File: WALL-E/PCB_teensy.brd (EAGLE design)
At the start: 128 x 109 mm, 44 parts

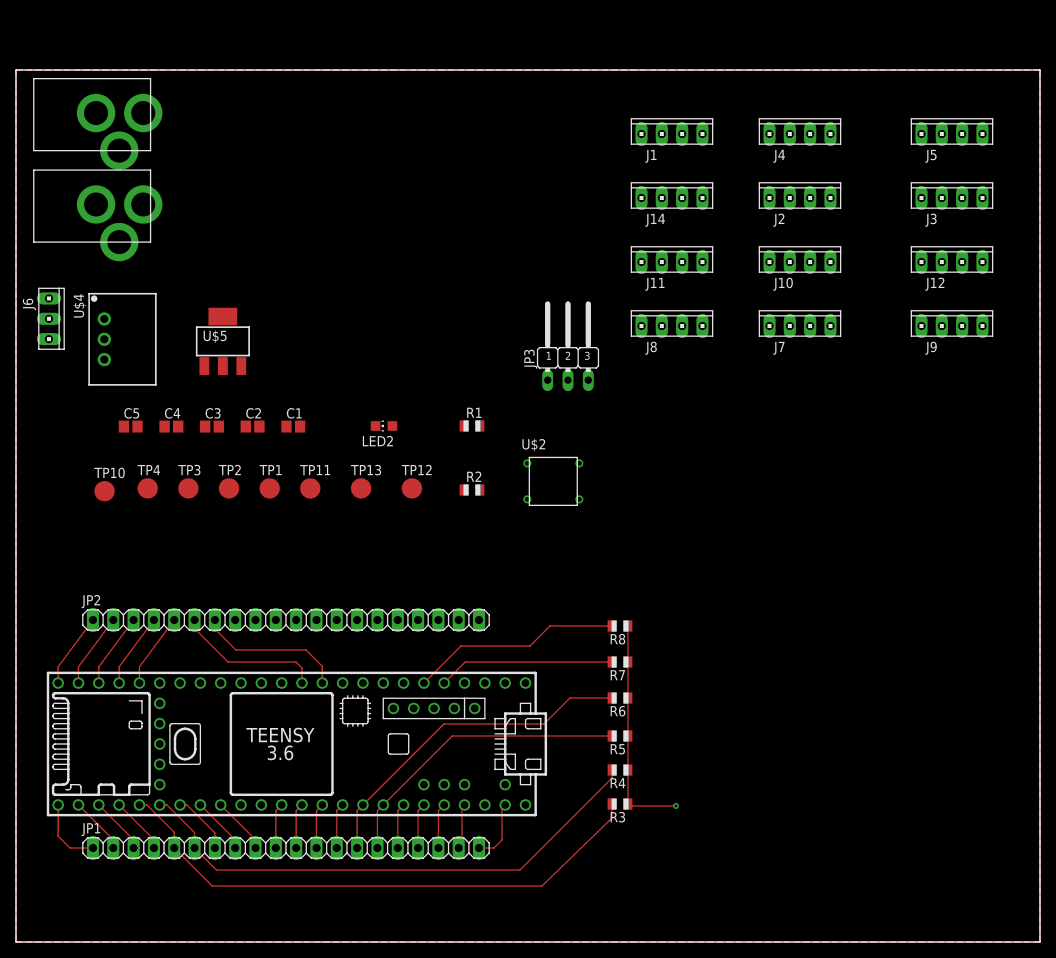
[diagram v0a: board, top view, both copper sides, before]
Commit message: Finished wiring the layers besides the tactile switch.
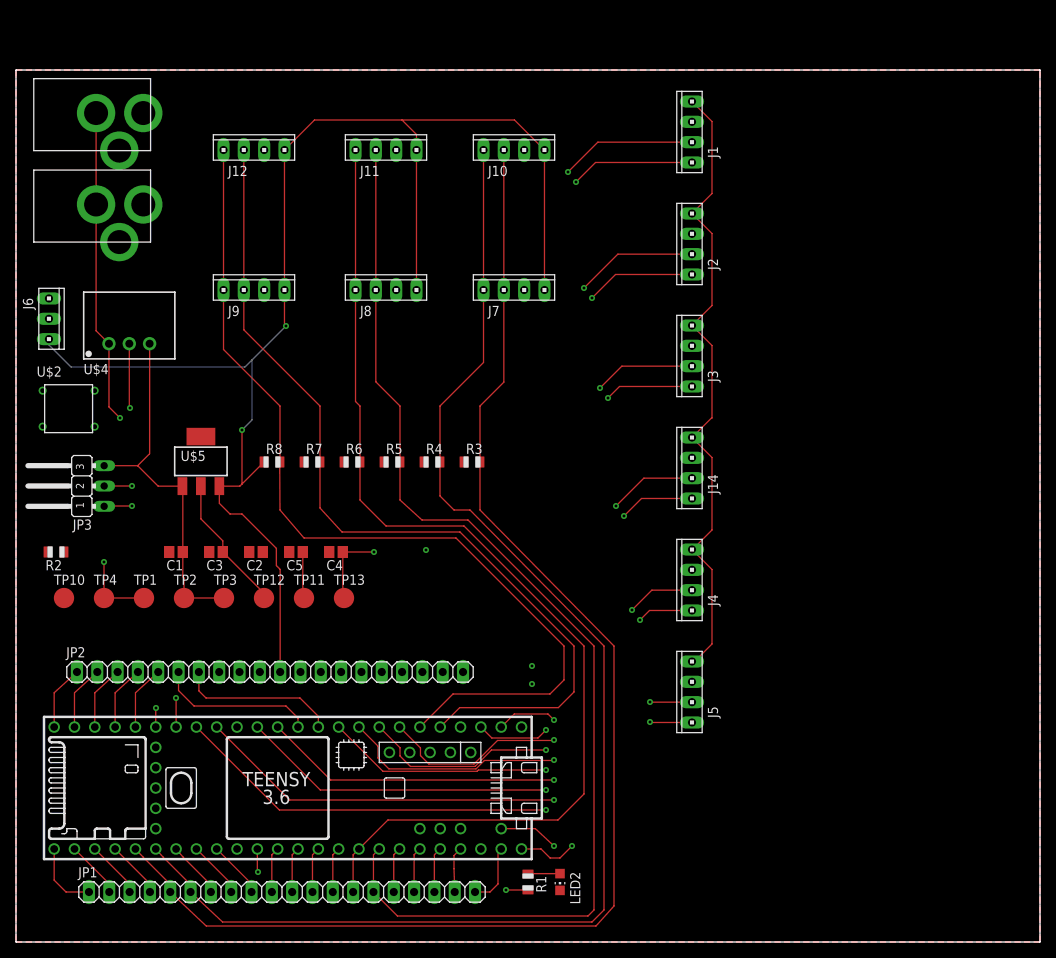
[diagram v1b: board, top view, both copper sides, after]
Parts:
- moved J12 88.4 mm to (29.8, 99.0)
- moved J9 87.4 mm to (29.8, 81.5)
- moved J5 77.0 mm to (84.5, 31.2), turned to 90 degrees
- moved U$2 61.3 mm to (3.58, 63.7)
- moved LED2 61.1 mm to (68.0, 7.50), turned to 180 degrees
- moved JP3 61.0 mm to (9.75, 57.0), turned to 90 degrees
- moved R1 57.4 mm to (64.0, 7.50), turned to 270 degrees
- moved J4 57.4 mm to (84.5, 45.2), turned to 90 degrees
- moved R2 52.6 mm to (5.00, 48.8), turned to 180 degrees
- moved R8 48.1 mm to (32.0, 60.0), turned to 0 degrees
- moved R3 46.6 mm to (57.0, 60.0), turned to 0 degrees
- moved R7 45.9 mm to (37.0, 60.0), turned to 0 degrees
- moved R4 45.1 mm to (52.0, 60.0), turned to 0 degrees
- moved R6 44.6 mm to (42.0, 60.0), turned to 0 degrees
- moved R5 44.6 mm to (47.0, 60.0), turned to 0 degrees
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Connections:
- net 10U renamed 10CS
- net 14U renamed A0
- net 15U renamed A1
- net 16U renamed A2
- net 17U renamed A3
- net 20U renamed A6
- net 21U renamed A7
- net 22U renamed A8
- net 23U renamed A9
- net 31U renamed A12
- net 32U renamed A13
- net 9U renamed 9CS
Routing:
- net 3.3V: track 28.4 -> 261.5 mm, vias 1 -> 2
- net SCL0: track 37.8 -> 144.5 mm
- net SDA1: track 66.8 -> 167.8 mm
- net VIN: track 0.00 -> 98.9 mm, vias 0 -> 2
- net SCL1: track 69.6 -> 168.0 mm
- net 6: track 0.00 -> 97.7 mm, vias 0 -> 2
- net 5: track 0.00 -> 96.3 mm, vias 0 -> 2
- net ALARMPIN: track 0.00 -> 95.5 mm, vias 0 -> 1
- net 1/TX: track 0.00 -> 95.4 mm, vias 0 -> 2
- net N$2: track 0.00 -> 95.4 mm, vias 0 -> 2
- net 0/RX: track 0.00 -> 94.4 mm, vias 0 -> 2
- net SDA0: track 42.4 -> 134.7 mm
- net 8: track 0.00 -> 90.0 mm, vias 0 -> 2
- net SCL2: track 22.1 -> 111.9 mm
- net 7: track 0.00 -> 89.4 mm, vias 0 -> 2
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
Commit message: finished routing
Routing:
- net N$4: track 0.00 -> 74.1 mm
- net N$5: track 5.81 -> 53.1 mm, vias 0 -> 2
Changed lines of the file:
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@@
 <?xml version="1.0" encoding="utf-8"?>
 <!DOCTYPE eagle SYSTEM "eagle.dtd">
-<eagle version="8.6.0">
+<eagle version="8.6.3">
 <drawing>
 <settings>
@@
 <vertex x="128" y="0"/>
 </polygon>
-<wire x1="9.83" y1="68.92" x2="9.83" y2="64.42" width="0" layer="19" extent="1-1"/>
 </signal>
 <signal name="5V">
@@
 <contactref element="TP10" pad="TP"/>
 <contactref element="U$1" pad="RESET"/>
-<wire x1="6" y1="48.75" x2="3.33" y2="68.92" width="0" layer="19" extent="1-1"/>
-<wire x1="6" y1="43" x2="6" y2="48.75" width="0" layer="19" extent="1-1"/>
-<wire x1="17.47" y1="14.17" x2="6" y2="43" width="0" layer="19" extent="1-1"/>
+<wire x1="6" y1="43" x2="2.25" y2="39.25" width="0.1524" layer="1"/>
+<wire x1="2.25" y1="14.5" x2="2.75" y2="14" width="0.1524" layer="1"/>
+<wire x1="2.75" y1="14" x2="17.3" y2="14" width="0.1524" layer="1"/>
+<wire x1="17.3" y1="14" x2="17.47" y2="14.17" width="0.1524" layer="1"/>
+<wire x1="2.25" y1="39.25" x2="2.25" y2="14.5" width="0.1524" layer="1"/>
+<wire x1="6" y1="43" x2="6" y2="48.75" width="0.1524" layer="1"/>
+<wire x1="6" y1="48.75" x2="1.5" y2="53.25" width="0.1524" layer="1"/>
+<wire x1="1.5" y1="67.09" x2="3.33" y2="68.92" width="0.1524" layer="1"/>
+<wire x1="1.5" y1="53.25" x2="1.5" y2="67.09" width="0.1524" layer="1"/>
 </signal>
 <signal name="N$5">
@@
 <wire x1="35.85" y1="48.75" x2="35.85" y2="43.15" width="0.1524" layer="1"/>
 <wire x1="35.85" y1="43.15" x2="36" y2="43" width="0.1524" layer="1"/>
-<wire x1="3.33" y1="64.42" x2="35.85" y2="48.75" width="0" layer="19" extent="1-1"/>
+<wire x1="3.33" y1="64.42" x2="3.33" y2="54.67" width="0.1524" layer="1"/>
+<wire x1="3.33" y1="54.67" x2="5.5" y2="52.5" width="0.1524" layer="1"/>
+<via x="5.5" y="52.5" extent="1-16" drill="0.35"/>
+<wire x1="5.5" y1="52.5" x2="28" y2="52.5" width="0.1524" layer="15"/>
+<wire x1="28" y1="52.5" x2="30.5" y2="55" width="0.1524" layer="15"/>
+<via x="30.5" y="55" extent="1-16" drill="0.35"/>
+<wire x1="30.5" y1="55" x2="35.85" y2="49.65" width="0.1524" layer="1"/>
+<wire x1="35.85" y1="49.65" x2="35.85" y2="48.75" width="0.1524" layer="1"/>
 </signal>
 <signal name="3.3V">
@@
 <wire x1="28.25" y1="57.25" x2="27.9812" y2="56.9812" width="0.1524" layer="1"/>
 <wire x1="4.12" y1="74.63" x2="4.12" y2="75.36" width="0.1524" layer="16"/>
-<wire x1="32.55" y1="47.05" x2="33.02" y2="46.58" width="0.1524" layer="1"/>
-<wire x1="33.02" y1="46.58" x2="33.02" y2="33.75" width="0.1524" layer="1"/>
+<wire x1="33.02" y1="46.58" x2="33.02" y2="46.5" width="0.1524" layer="1"/>
+<wire x1="33.02" y1="46.5" x2="33.02" y2="33.75" width="0.1524" layer="1"/>
 <wire x1="28.625" y1="71.875" x2="6.875" y2="71.875" width="0.1524" layer="16"/>
 <wire x1="6.875" y1="71.875" x2="4.12" y2="74.63" width="0.1524" layer="16"/>
 <wire x1="29.5" y1="72.75" x2="29.5" y2="65.25" width="0.1524" layer="16"/>
 <wire x1="29.5" y1="65.25" x2="28.25" y2="64" width="0.1524" layer="16"/>
-<wire x1="32.55" y1="47.05" x2="32.55" y2="49.2" width="0.1524" layer="1"/>
-<wire x1="32.55" y1="49.2" x2="28.25" y2="53.5" width="0.1524" layer="1"/>
-<wire x1="28.25" y1="53.5" x2="26.75" y2="53.5" width="0.1524" layer="1"/>
+<wire x1="26.75" y1="53.5" x2="28.25" y2="53.5" width="0.1524" layer="1"/>
 <wire x1="26.75" y1="53.5" x2="25.4214" y2="54.8286" width="0.1524" layer="1"/>
 <wire x1="25.4214" y1="54.8286" x2="25.4214" y2="56.9812" width="0.1524" layer="1"/>
@@
 <wire x1="48.25" y1="102.75" x2="50.06" y2="100.94" width="0.1524" layer="1"/>
 <wire x1="50.06" y1="100.94" x2="50.06" y2="99" width="0.1524" layer="1"/>
-<wire x1="66.03" y1="99.03" x2="62.31" y2="102.75" width="0.1524" layer="1"/>
+<wire x1="66.06" y1="99" x2="62.31" y2="102.75" width="0.1524" layer="1"/>
 <wire x1="62.31" y1="102.75" x2="48.25" y2="102.75" width="0.1524" layer="1"/>
 <wire x1="50.06" y1="99" x2="50.06" y2="81.5" width="0.1524" layer="1"/>
@@
 <wire x1="84.81" y1="35.06" x2="84.5" y2="35.06" width="0.1524" layer="1"/>
 <wire x1="66.06" y1="81.5" x2="66.06" y2="99" width="0.1524" layer="1"/>
-<wire x1="66.06" y1="99" x2="66.03" y2="99.03" width="0.1524" layer="1"/>
-<wire x1="51" y1="60" x2="56" y2="60" width="0" layer="19" extent="1-1"/>
-<wire x1="46" y1="60" x2="51" y2="60" width="0" layer="19" extent="1-1"/>
-<wire x1="41" y1="60" x2="46" y2="60" width="0" layer="19" extent="1-1"/>
-<wire x1="36" y1="60" x2="41" y2="60" width="0" layer="19" extent="1-1"/>
-<wire x1="31" y1="60" x2="36" y2="60" width="0" layer="19" extent="1-1"/>
-<wire x1="30.85" y1="48.75" x2="32.55" y2="49.2" width="0" layer="19" extent="1-1"/>
-<wire x1="4" y1="48.75" x2="25.4214" y2="54.8286" width="0" layer="19" extent="1-1"/>
+<wire x1="33.02" y1="46.5" x2="30.85" y2="48.67" width="0.1524" layer="1"/>
+<wire x1="30.85" y1="48.67" x2="30.85" y2="48.75" width="0.1524" layer="1"/>
+<wire x1="28.25" y1="53.5" x2="30.85" y2="50.9" width="0.1524" layer="1"/>
+<wire x1="30.85" y1="50.9" x2="30.85" y2="48.75" width="0.1524" layer="1"/>
 </signal>
 <signal name="N$8">

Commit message: jk now routing is finished
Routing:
- net 3.3V: track 261.6 -> 342.3 mm, vias 2 -> 8
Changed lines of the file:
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@@
 <wire x1="28.25" y1="53.5" x2="30.85" y2="50.9" width="0.1524" layer="1"/>
 <wire x1="30.85" y1="50.9" x2="30.85" y2="48.75" width="0.1524" layer="1"/>
+<wire x1="56" y1="60" x2="56" y2="62.5" width="0.1524" layer="1"/>
+<wire x1="56" y1="62.5" x2="55" y2="63.5" width="0.1524" layer="1"/>
+<wire x1="55" y1="63.5" x2="55" y2="63.25" width="0.1524" layer="1"/>
+<via x="55" y="63.25" extent="1-16" drill="0.35"/>
+<wire x1="55" y1="63.25" x2="50.75" y2="63.25" width="0.1524" layer="16"/>
+<wire x1="50.75" y1="63.25" x2="50.5" y2="63.5" width="0.1524" layer="16"/>
+<via x="50.5" y="63.5" extent="1-16" drill="0.35"/>
+<wire x1="50.5" y1="63.5" x2="50.5" y2="60.5" width="0.1524" layer="1"/>
+<wire x1="50.5" y1="60.5" x2="51" y2="60" width="0.1524" layer="1"/>
+<wire x1="50.5" y1="63.5" x2="46" y2="63.5" width="0.1524" layer="16"/>
+<via x="46" y="63.5" extent="1-16" drill="0.35"/>
+<wire x1="46" y1="63.5" x2="46" y2="60" width="0.1524" layer="1"/>
+<wire x1="46" y1="63.5" x2="41" y2="63.5" width="0.1524" layer="16"/>
+<via x="41" y="63.5" extent="1-16" drill="0.35"/>
+<wire x1="41" y1="63.5" x2="41" y2="60" width="0.1524" layer="1"/>
+<wire x1="41" y1="63.5" x2="36" y2="63.5" width="0.1524" layer="16"/>
+<via x="36" y="63.5" extent="1-16" drill="0.35"/>
+<wire x1="36" y1="63.5" x2="36" y2="60" width="0.1524" layer="1"/>
+<wire x1="36" y1="63.5" x2="28.75" y2="63.5" width="0.1524" layer="16"/>
+<wire x1="28.75" y1="63.5" x2="28.25" y2="64" width="0.1524" layer="16"/>
+<wire x1="4" y1="48.75" x2="1.75" y2="46.5" width="0.1524" layer="1"/>
+<wire x1="1.75" y1="46.5" x2="1.75" y2="41.75" width="0.1524" layer="1"/>
+<via x="1.75" y="41.75" extent="1-16" drill="0.35"/>
+<wire x1="1.75" y1="41.75" x2="5.5" y2="38" width="0.1524" layer="16"/>
+<wire x1="5.5" y1="38" x2="21.75" y2="38" width="0.1524" layer="16"/>
+<wire x1="21.75" y1="38" x2="25.4" y2="34.35" width="0.1524" layer="16"/>
+<wire x1="25.4" y1="34.35" x2="25.4" y2="33.75" width="0.1524" layer="16"/>
 </signal>
 <signal name="N$8">

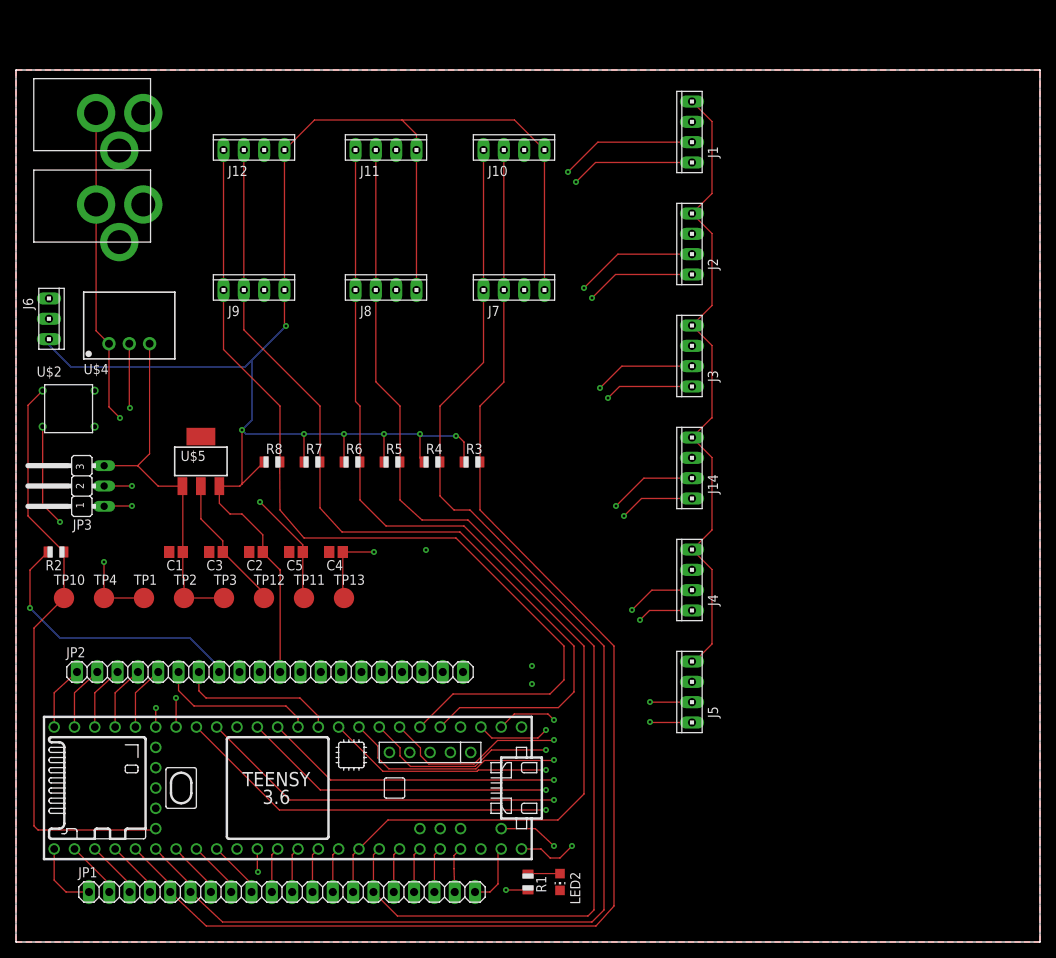
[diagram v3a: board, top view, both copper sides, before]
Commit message: resized the board
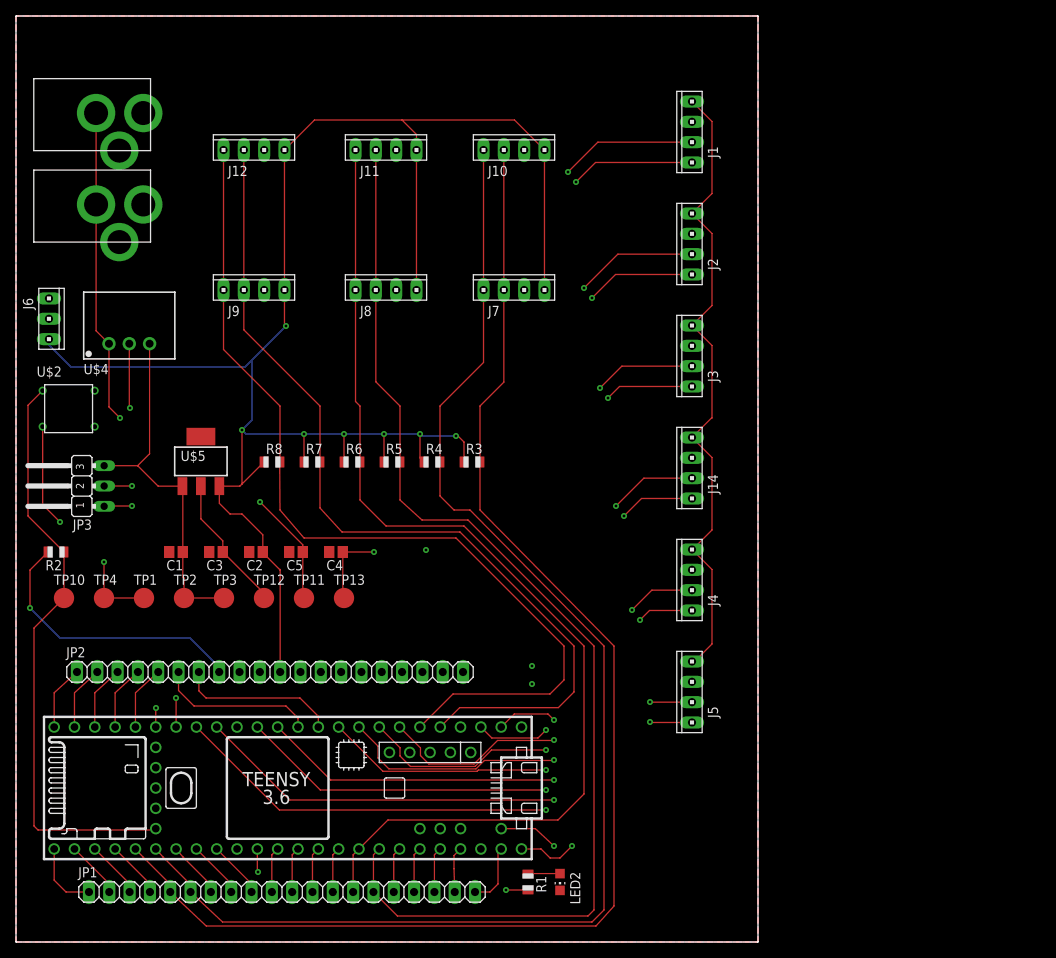
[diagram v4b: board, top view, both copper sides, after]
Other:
- board size 128 x 109 mm -> 92.8 x 115.8 mm
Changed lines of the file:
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@@
 <board>
 <plain>
-<wire x1="0" y1="0" x2="128" y2="0" width="0" layer="20"/>
-<wire x1="128" y1="0" x2="128" y2="109" width="0" layer="20"/>
-<wire x1="128" y1="109" x2="0" y2="109" width="0" layer="20"/>
-<wire x1="0" y1="109" x2="0" y2="0" width="0" layer="20"/>
-<dimension x1="0" y1="109" x2="0" y2="0" x3="0" y3="54.5" textsize="1.778" layer="1" dtype="horizontal"/>
-<dimension x1="0" y1="0" x2="0" y2="109" x3="0" y3="54.5" textsize="1.778" layer="1" dtype="vertical"/>
+<wire x1="0" y1="0" x2="92.75" y2="0" width="0" layer="20"/>
+<wire x1="92.75" y1="0" x2="92.75" y2="115.75" width="0" layer="20"/>
+<wire x1="92.75" y1="115.75" x2="0" y2="115.75" width="0" layer="20"/>
+<wire x1="0" y1="115.75" x2="0" y2="0" width="0" layer="20"/>
+<dimension x1="0" y1="115.75" x2="0" y2="0" x3="0" y3="57.875" textsize="1.778" layer="1" dtype="horizontal"/>
+<dimension x1="0" y1="0" x2="0" y2="115.75" x3="0" y3="57.875" textsize="1.778" layer="1" dtype="vertical"/>
 </plain>
 <attributes>
@@
 <polygon width="0.1524" layer="1">
 <vertex x="0" y="0"/>
-<vertex x="128" y="0"/>
-<vertex x="128" y="109"/>
-<vertex x="0" y="109"/>
+<vertex x="92.75" y="0"/>
+<vertex x="92.75" y="115.75"/>
+<vertex x="0" y="115.75"/>
 </polygon>
 <polygon width="0.1524" layer="1">
 <vertex x="0" y="0"/>
-<vertex x="0" y="109"/>
-<vertex x="128" y="109"/>
-<vertex x="128" y="0"/>
+<vertex x="0" y="115.75"/>
+<vertex x="92.75" y="115.75"/>
+<vertex x="92.75" y="0"/>
 </polygon>
 </signal>
@@
 <polygon width="0.1524" layer="16">
 <vertex x="0" y="0"/>
-<vertex x="128" y="0"/>
-<vertex x="128" y="109"/>
-<vertex x="0" y="109"/>
+<vertex x="92.75" y="0"/>
+<vertex x="92.75" y="115.75"/>
+<vertex x="0" y="115.75"/>
 </polygon>
 <wire x1="31" y1="60" x2="28.25" y2="57.25" width="0.1524" layer="1"/>

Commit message: Added silkscreen to alarm pin and shifted the components to the top right for more silkscreen real estate.
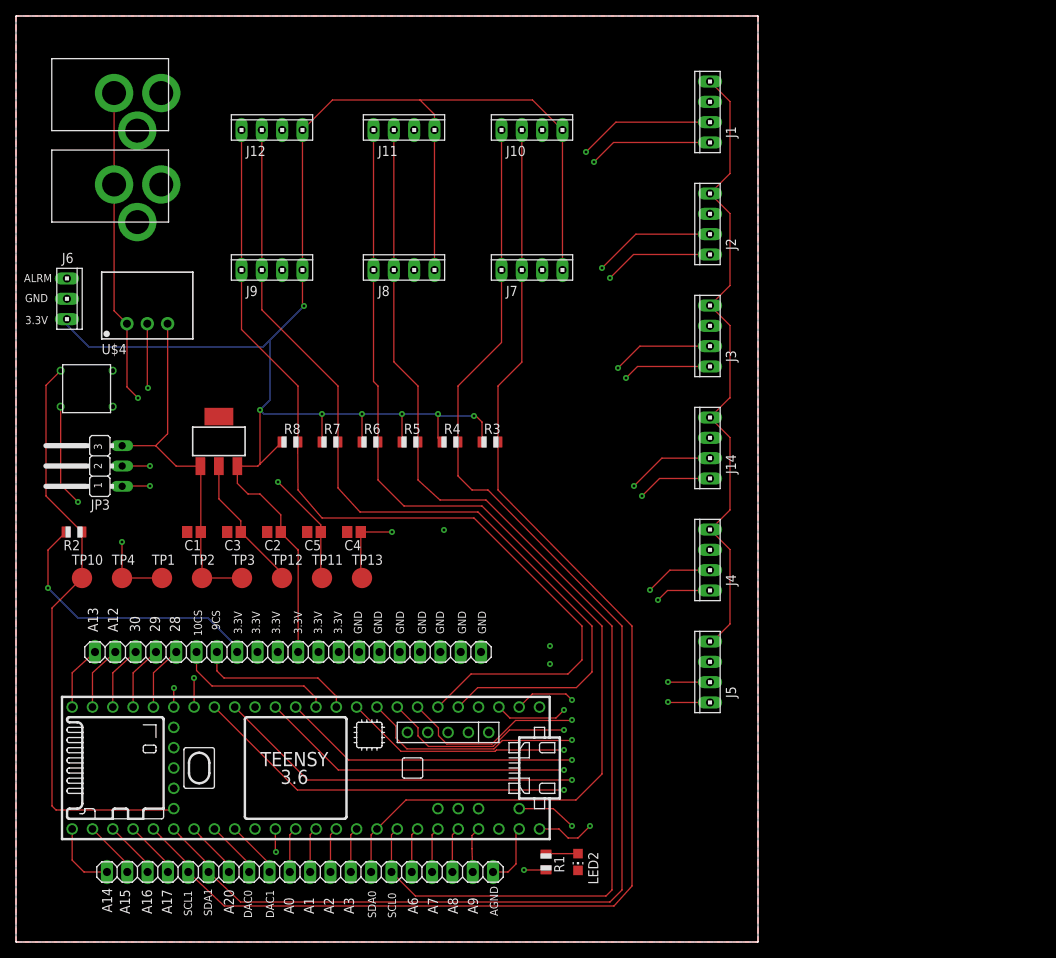
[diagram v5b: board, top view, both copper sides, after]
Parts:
- moved C1 3.36 mm to (22.2, 51.2)
- moved C2 3.36 mm to (32.2, 51.2)
- moved C3 3.36 mm to (27.2, 51.2)
- moved C4 3.36 mm to (42.2, 51.2)
- moved C5 3.36 mm to (37.2, 51.2)
- moved J1 3.36 mm to (86.8, 103.8)
- moved J10 3.36 mm to (64.5, 101.5)
- moved J11 3.36 mm to (48.5, 101.5)
- moved J12 3.36 mm to (32.0, 101.5)
- moved J14 3.36 mm to (86.8, 61.8)
- moved J2 3.36 mm to (86.8, 89.8)
- moved J3 3.36 mm to (86.8, 75.8)
- moved J4 3.36 mm to (86.8, 47.8)
- moved J5 3.36 mm to (86.8, 33.8)
- moved J6 3.36 mm to (6.37, 80.4)
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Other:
- board text added: "10CS"
- board text added: "28"
- board text added: "29"
- board text added: "3.3V"
- board text added: "30"
- board text added: "9CS"
- board text added: "A0"
- board text added: "A1"
- board text added: "A12"
- board text added: "A13"
- board text added: "A14"
- board text added: "A15"
- board text added: "A16"
- board text added: "A17"
- board text added: "A2"
- board text added: "A20"
- board text added: "A3"
- board text added: "A6"
- board text added: "A7"
- board text added: "A8"
- board text added: "A9"
- board text added: "AGND"
- board text added: "ALRM"
- board text added: "DAC0"
- board text added: "DAC1"
- board text added: "GND"
- board text added: "SCL0"
- board text added: "SCL1"
- board text added: "SDA0"
- board text added: "SDA1"
